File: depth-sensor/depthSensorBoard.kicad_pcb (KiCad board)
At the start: 2 copper layers, 76.2 x 48.3 mm, 28 parts, among them IC1 ATMEGA1284P-M, M1 MountingHole_3.5mm, M2 MountingHole_3.5mm, M3 MountingHole_3.5mm, M4 MountingHole_3.5mm, P1 CONN_02X05, P2 CONN_02X03, P3 CONN_01X04, P4 CONN_01X04, P5 CONN_01X04, P6 CONN_01X04, Q2 Q_NJFET_GSD, U1 AP2112, U2 TCA9545A, Y1 16MHz

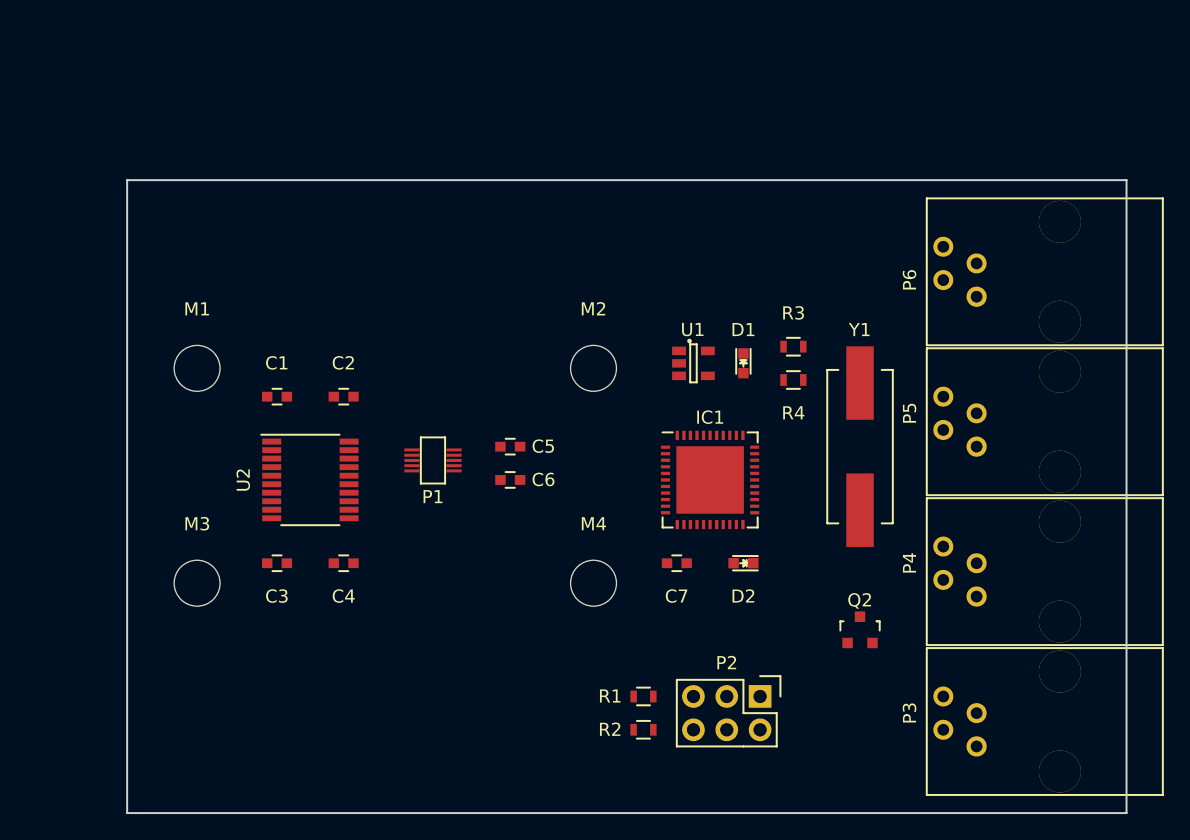
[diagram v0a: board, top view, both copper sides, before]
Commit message: Made PCB smaller
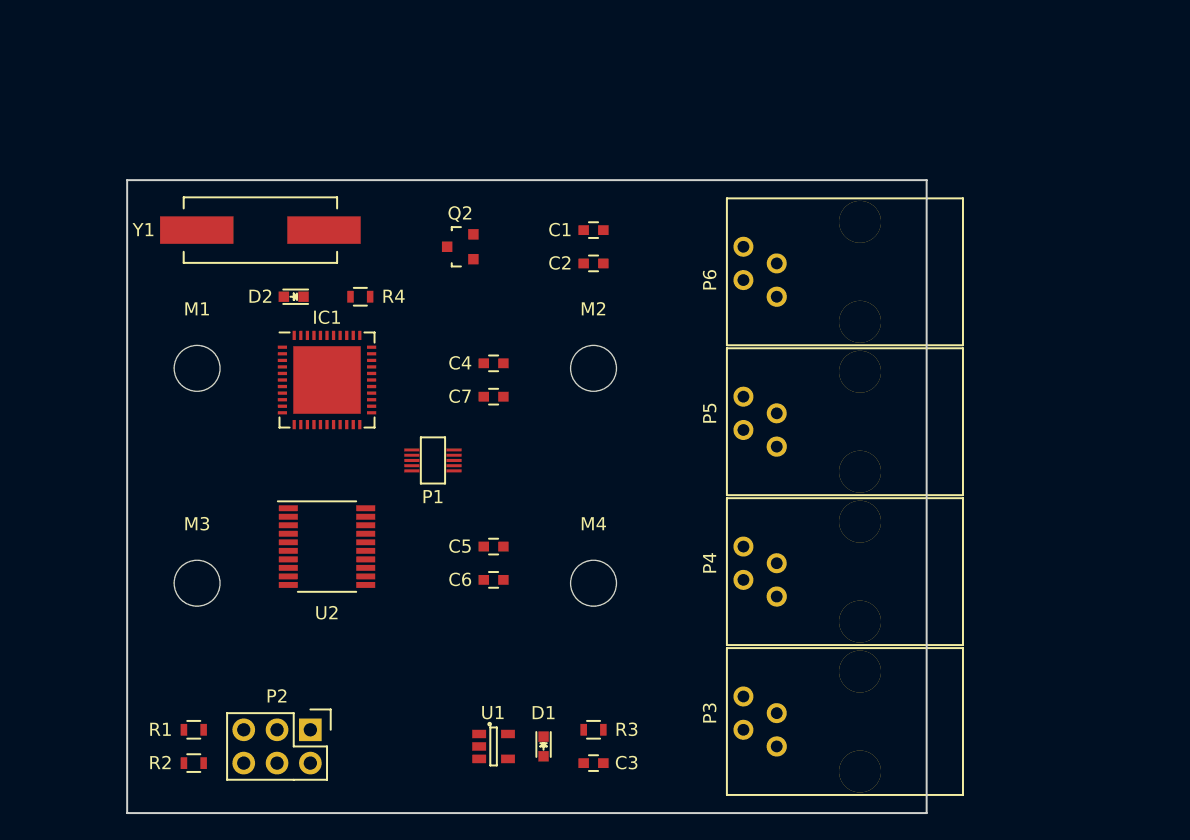
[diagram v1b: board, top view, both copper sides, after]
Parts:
- moved Y1 48.6 mm to (118.1, 110.5), turned to 180 degrees
- moved Q2 42.2 mm to (133.3, 111.8), turned to 90 degrees
- moved D2 39.9 mm to (120.7, 115.6)
- moved P2 34.4 mm to (121.9, 148.6)
- moved R1 34.4 mm to (113.0, 148.6)
- moved R2 34.4 mm to (113.0, 151.1)
- moved R4 33.6 mm to (125.7, 115.6)
- moved D1 32.9 mm to (139.7, 149.9)
- moved R3 32.9 mm to (143.5, 148.6)
- moved U1 32.9 mm to (135.9, 149.9)
- moved IC1 30.2 mm to (123.2, 121.9)
- moved C3 28.5 mm to (143.5, 151.1)
- moved C1 27.3 mm to (143.5, 110.5), turned to 180 degrees
- moved C2 21.6 mm to (143.5, 113.0), turned to 180 degrees
- moved C4 19.0 mm to (135.9, 120.7), turned to 180 degrees
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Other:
- board size 76.2 x 48.3 mm -> 61 x 48.3 mm

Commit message: Rearranged PCB, removed LEDs from depth sensor schematic
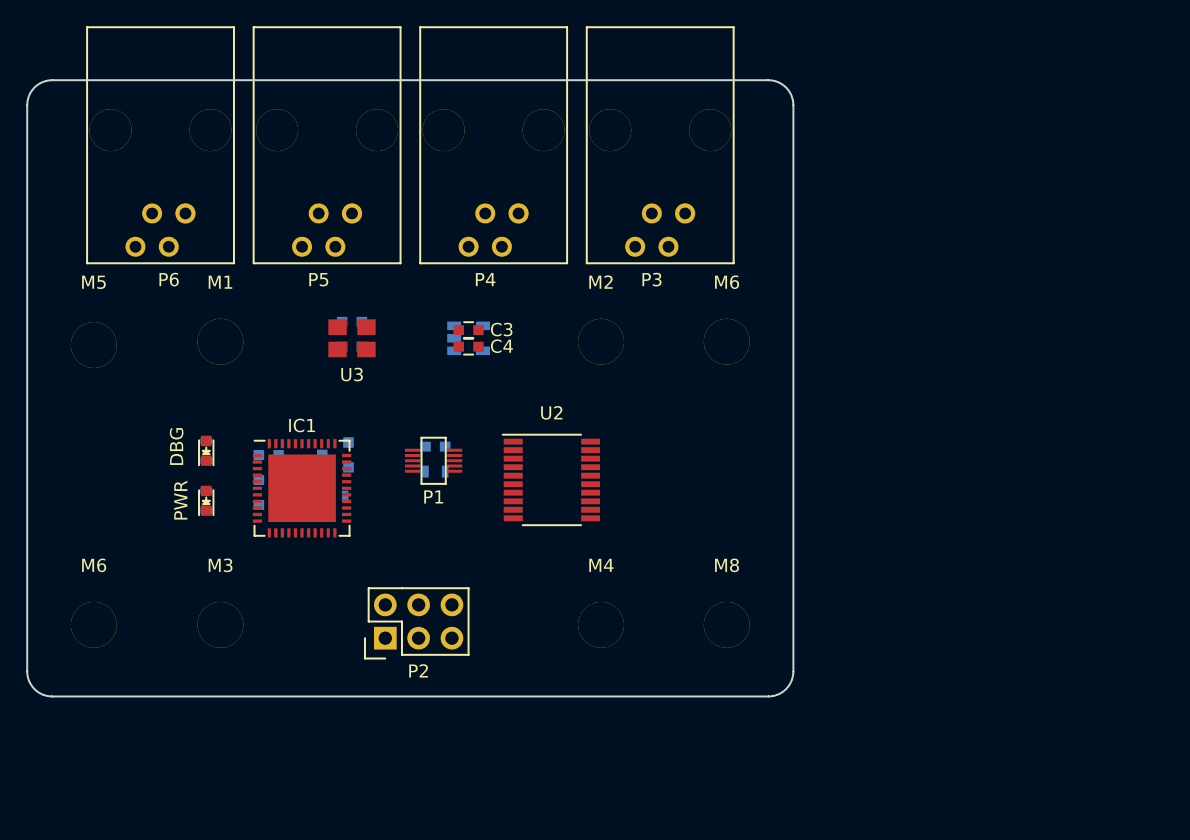
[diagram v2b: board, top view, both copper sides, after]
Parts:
- removed D1, D2: LED, LEDs:LED_0603
- removed R3, R4: 66.5, Resistors_SMD:R_0603
- removed Y1: 16MHz, Crystals:Crystal_HC49-SD_SMD
- added C8: 4.7u, Capacitors_SMD:C_0603, B.Cu at (118.7, 131.4)
- added DBG: LED, LEDs:LED_0603, F.Cu at (114.0, 127.3)
- added M5: MountingHole_3.5mm, Mounting_Holes:MountingHole_3.5mm, F.Cu at (105.4, 119.0)
- added M6: MountingHole_3.5mm, Mounting_Holes:MountingHole_3.5mm, F.Cu at (153.7, 119.0)
- added M6: MountingHole_3.5mm, Mounting_Holes:MountingHole_3.5mm, F.Cu at (105.4, 140.6)
- added M8: MountingHole_3.5mm, Mounting_Holes:MountingHole_3.5mm, F.Cu at (153.7, 140.6)
- added PWR: LED, LEDs:LED_0603, F.Cu at (114.0, 131.1)
- added R5: 65, Resistors_SMD:R_0603, B.Cu at (114.0, 131.1)
- added R6: 65, Resistors_SMD:R_0603, B.Cu at (114.0, 127.3)
- added U3: TSX-3225, robosub_footprints:DFN-4, F.Cu at (125.1, 118.7)
- C1: value 0.1μF -> 100nF; moved to B.Cu
- C2: value 0.1μF -> 18p; moved to B.Cu
- C5: value 100nF -> 18p; moved to B.Cu
- C6, C7: value 30pF -> 100n; moved to B.Cu
- P1: value CONN_02X05 -> Mezzanine-Header
- Q2, R1, R2, U1: moved to B.Cu
- moved P6 45.5 mm to (112.4, 109.2), turned to 180 degrees
- moved P3 41.2 mm to (150.5, 109.2), turned to 180 degrees
- moved P5 36.9 mm to (125.1, 109.2), turned to 180 degrees
- moved P4 35.2 mm to (137.8, 109.2), turned to 180 degrees
- moved C3 34.4 mm to (134.0, 118.1)
- moved U1 31.2 mm to (134.0, 118.7)
- moved R1 27.0 mm to (131.4, 128.9)
- moved R2 23.0 mm to (123.8, 130.8)
- moved C1 20.4 mm to (131.4, 127.0)
- moved C6 19.6 mm to (118.7, 127.6)
- moved C2 18.9 mm to (125.1, 117.5)
- moved C5 18.7 mm to (125.1, 119.4)
- moved Q2 18.5 mm to (123.8, 127.6), turned to 270 degrees
- moved C7 18.3 mm to (118.7, 129.5)
- moved U2 17.9 mm to (140.3, 129.5)
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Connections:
- C1 pad 1: +5V -> Net-(C1-Pad1)
- C1 pad 2: GND -> /DTR
- C2 pad 1: +5V -> Net-(C2-Pad1)
- C5 pad 2: /DTR -> GND
- C6 pad 1: GND -> +5V
- C6 pad 2: Net-(C6-Pad2) -> GND
- C7 pad 1: Net-(C7-Pad1) -> +5V
- IC1 pad 7: Net-(C6-Pad2) -> Net-(C5-Pad1)
- IC1 pad 8: Net-(C7-Pad1) -> Net-(C2-Pad1)
- P3 pad 2: /SCL2 -> /SCL0
- P3 pad 3: /SDA2 -> /SDA0
- P4 pad 2: /SCL3 -> /SCL1
- P4 pad 3: /SDA3 -> /SDA1
- P5 pad 2: /SCL0 -> /SCL2
- P5 pad 3: /SDA0 -> /SDA2
- P6 pad 2: /SCL1 -> /SCL3
- P6 pad 3: /SDA1 -> /SDA3
- R1 pad 2: Net-(C5-Pad1) -> Net-(C1-Pad1)
- R2 pad 2: Net-(C5-Pad1) -> Net-(C1-Pad1)
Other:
- board size 61 x 48.3 mm -> 58.4 x 47 mm

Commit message: Routing completed
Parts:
- moved DBG 0.45 mm to (113.7, 127.0)
- moved PWR 0.45 mm to (113.7, 131.4)
- moved R5 0.45 mm to (113.7, 131.4)
- moved R6 0.45 mm to (113.7, 127.0)
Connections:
- C6 pad 1: +5V -> +3V3
- C7 pad 1: +5V -> +3V3
- C8 pad 1: +5V -> +3V3
- DBG pad 2: /ATMega1284p/DBG_LED -> /DBG_LED
- IC1 pad 17: +5V -> +3V3
- IC1 pad 27: +5V -> +3V3
- IC1 pad 33: /D_LED -> /DBG_LED
- IC1 pad 38: +5V -> +3V3
- IC1 pad 5: +5V -> +3V3
- P2 pad 2: +5V -> +3V3
- PWR pad 2: +5V -> +3V3
- R1 pad 1: +5V -> +3V3
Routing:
- net +3V3: track 0.00 -> 158.3 mm, vias 0 -> 12
- net GND: track 0.00 -> 88.3 mm, vias 0 -> 8
- net /drn: track 0.00 -> 63.8 mm, vias 0 -> 5
- net /SDA3: track 0.00 -> 59.7 mm
- net /SCL3: track 0.00 -> 53.9 mm
- net /SDA2: track 0.00 -> 50.3 mm
- net /SCL2: track 0.00 -> 49.0 mm, vias 0 -> 4
- net /ATMega1284p/SCK: track 0.00 -> 46.3 mm, vias 0 -> 2
- net /ATMega1284p/MISO: track 0.00 -> 46.2 mm
- net /ATMega1284p/~RST: track 0.00 -> 38.9 mm, vias 0 -> 2
- net /~INT: track 0.00 -> 36.7 mm
- net /SCL: track 0.00 -> 35.2 mm, vias 0 -> 2
- net /SDA: track 0.00 -> 32.5 mm, vias 0 -> 2
- net /ATMega1284p/MOSI: track 0.00 -> 29.6 mm, vias 0 -> 4
- net /SCL1: track 0.00 -> 29.6 mm, vias 0 -> 2
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- added copper zone on F.Cu, net +3V3
- added copper zone on B.Cu, net GND
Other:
- net class Default: clearance 0.2 -> 0.1524; trace_width 0.25 -> 0.1524; via_dia 0.6 -> 0.508; via_drill 0.4 -> 0.3302
- rule trace_clearance: 0.2 -> 0.1524
- rule trace_min: 0.2 -> 0.1524
- rule via_min_size: 0.4 -> 0.508

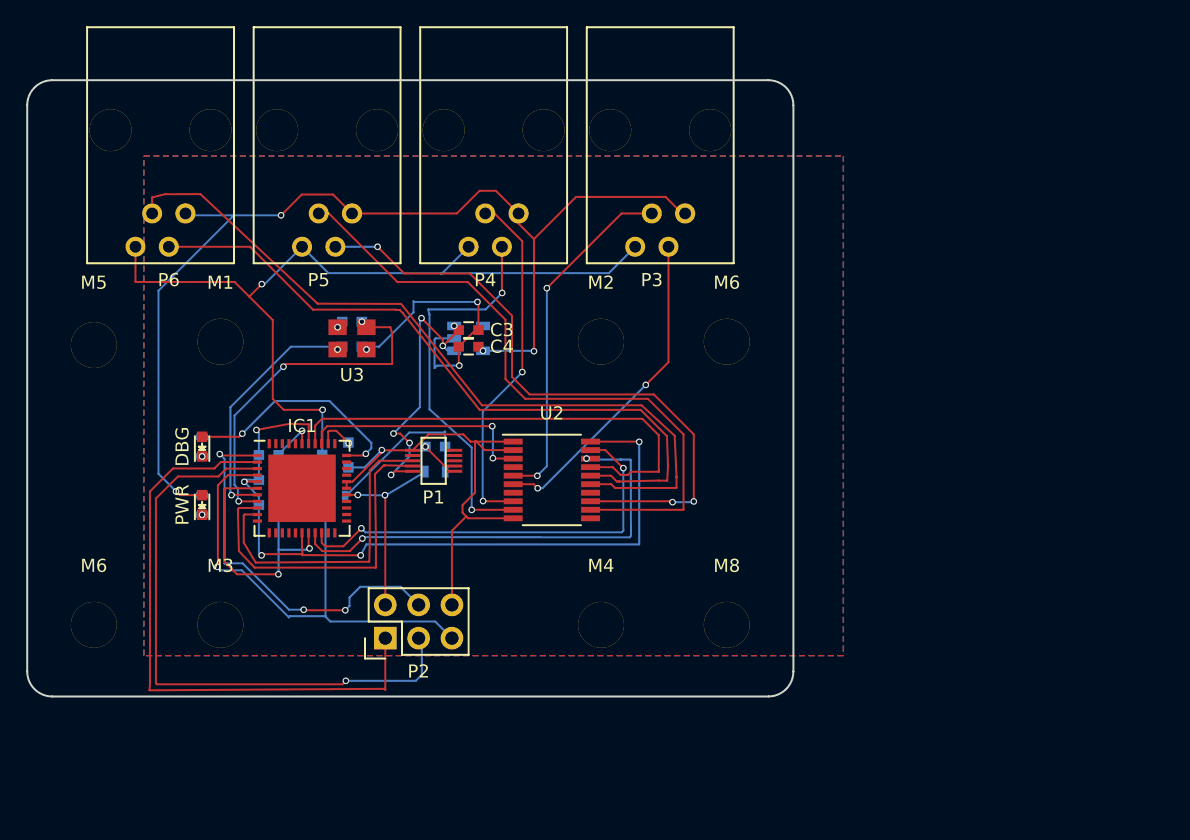
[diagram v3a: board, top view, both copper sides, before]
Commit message: Changed to just GND fill
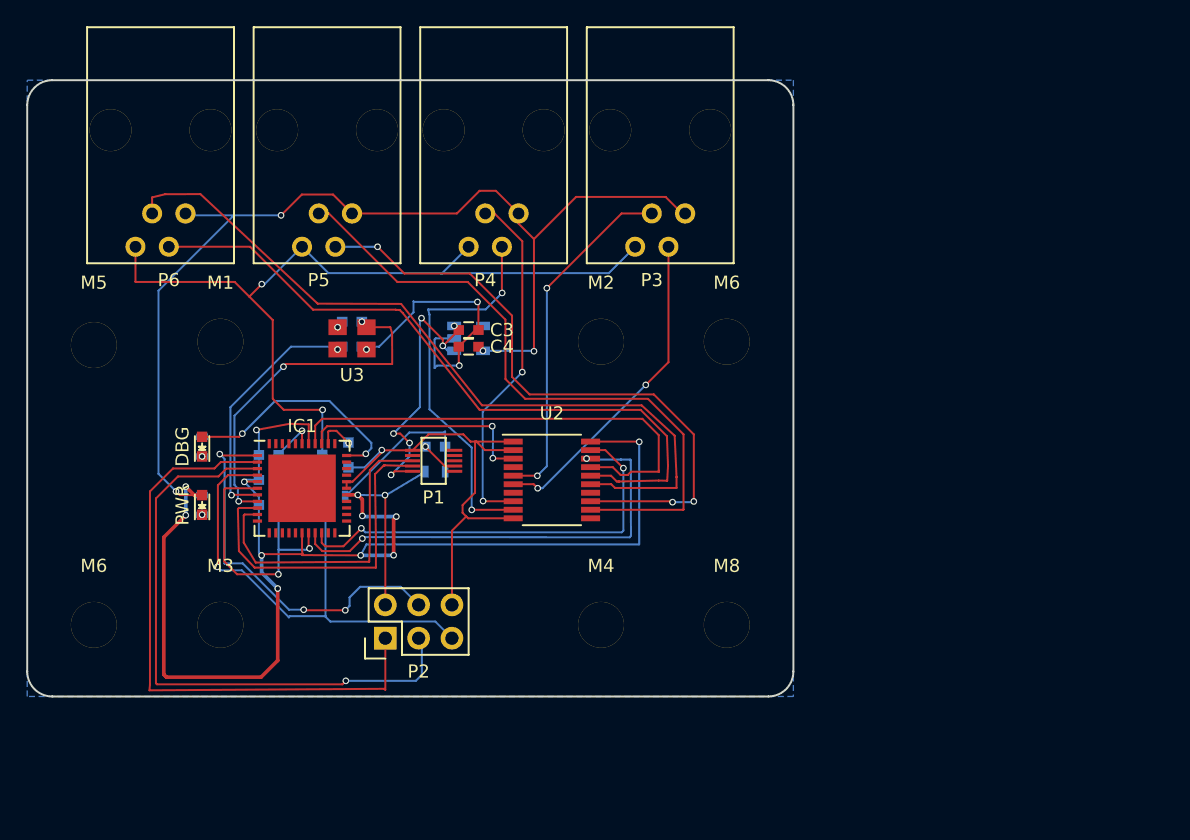
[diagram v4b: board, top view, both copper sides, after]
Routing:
- net +3V3: track 158.3 -> 202.6 mm, vias 12 -> 18
- removed copper zone on F.Cu, net +3V3
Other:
- net class PWR added: clearance 0.1524, trace_width 0.2788, via_dia 0.508, via_drill 0.3302
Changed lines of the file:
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@@
     (thickness 1.6)
     (drawings 10)
-    (tracks 478)
+    (tracks 503)
     (zones 0)
     (modules 33)
@@
     (uvia_dia 0.3)
     (uvia_drill 0.1)
-    (add_net +3V3)
-    (add_net +5V)
     (add_net /ATMega1284p/MISO)
     (add_net /ATMega1284p/MOSI)
@@
     (add_net /~INT)
     (add_net /~RST)
-    (add_net GND)
     (add_net "Net-(C1-Pad1)")
     (add_net "Net-(C2-Pad1)")
@@
     (add_net "Net-(U2-Pad4)")
     (add_net "Net-(U2-Pad7)")
+  )
+  (net_class PWR ""
+    (clearance 0.1524)
+    (trace_width 0.2788)
+    (via_dia 0.508)
+    (via_drill 0.3302)
+    (uvia_dia 0.3)
+    (uvia_drill 0.1)
+    (add_net +3V3)
+    (add_net +5V)
+    (add_net GND)
   )
   (module Resistors_SMD:R_0603 (layer B.Cu)
@@
   (via (at 121.285 125.7935) (size 0.508) (drill 0.3302) (layers F.Cu B.Cu) (net 2))
   (segment (start 119.495 127.5835) (end 119.495 127.635) (width 0.1524) (layer B.Cu) (net 2))
+  (segment (start 124.685 130.675) (end 125.5315 130.675) (width 0.2788) (layer F.Cu) (net 3))
+  (segment (start 125.5315 130.675) (end 125.8824 131.0259) (width 0.2788) (layer F.Cu) (net 3))
+  (segment (start 128.25984 135.29056) (end 125.76048 135.29056) (width 0.2788) (layer B.Cu) (net 3))
+  (segment (start 128.27 135.2804) (end 128.25984 135.29056) (width 0.2788) (layer B.Cu) (net 3))
+  (via (at 128.27 135.2804) (size 0.508) (drill 0.3302) (layers F.Cu B.Cu) (net 3))
+  (segment (start 128.27 132.5372) (end 128.27 135.2804) (width 0.2788) (layer F.Cu) (net 3))
+  (segment (start 128.4732 132.334) (end 128.27 132.5372) (width 0.2788) (layer F.Cu) (net 3))
+  (via (at 128.4732 132.334) (size 0.508) (drill 0.3302) (layers F.Cu B.Cu) (net 3))
+  (segment (start 125.9332 132.334) (end 128.4732 132.334) (width 0.2788) (layer B.Cu) (net 3))
+  (segment (start 125.8824 132.2832) (end 125.9332 132.334) (width 0.2788) (layer B.Cu) (net 3))
+  (via (at 125.8824 132.2832) (size 0.508) (drill 0.3302) (layers F.Cu B.Cu) (net 3))
+  (segment (start 125.8824 131.0259) (end 125.8824 132.2832) (width 0.2788) (layer F.Cu) (net 3))
+  (segment (start 113.665 130.6957) (end 113.0681 130.6957) (width 0.2788) (layer F.Cu) (net 3))
+  (segment (start 118.20144 136.59104) (end 118.20144 135.29056) (width 0.2788) (layer B.Cu) (net 3))
+  (segment (start 119.4308 137.8204) (end 118.20144 136.59104) (width 0.2788) (layer B.Cu) (net 3))
+  (via (at 119.4308 137.8204) (size 0.508) (drill 0.3302) (layers F.Cu B.Cu) (net 3))
+  (segment (start 119.4308 143.3068) (end 119.4308 137.8204) (width 0.2788) (layer F.Cu) (net 3))
+  (segment (start 118.1608 144.5768) (end 119.4308 143.3068) (width 0.2788) (layer F.Cu) (net 3))
+  (segment (start 110.9472 144.5768) (end 118.1608 144.5768) (width 0.2788) (layer F.Cu) (net 3))
+  (segment (start 110.744 144.3736) (end 110.9472 144.5768) (width 0.2788) (layer F.Cu) (net 3))
+  (segment (start 110.744 133.9088) (end 110.744 144.3736) (width 0.2788) (layer F.Cu) (net 3))
+  (segment (start 112.4204 132.2324) (end 110.744 133.9088) (width 0.2788) (layer F.Cu) (net 3))
+  (via (at 112.4204 132.2324) (size 0.508) (drill 0.3302) (layers F.Cu B.Cu) (net 3))
+  (segment (start 112.4204 130.048) (end 112.4204 132.2324) (width 0.2788) (layer B.Cu) (net 3))
+  (via (at 112.4204 130.048) (size 0.508) (drill 0.3302) (layers F.Cu B.Cu) (net 3))
+  (segment (start 113.0681 130.6957) (end 112.4204 130.048) (width 0.2788) (layer F.Cu) (net 3))
   (segment (start 113.665 130.6957) (end 111.96066 130.6957) (width 0.1524) (layer F.Cu) (net 3))
   (segment (start 110.3376 115.1128) (end 116.08816 109.36224) (width 0.1524) (layer B.Cu) (net 3))
@@
   (segment (start 111.96066 130.6957) (end 111.67872 130.41376) (width 0.1524) (layer F.Cu) (net 3))
   (segment (start 117.995 131.445) (end 117.995 135.08412) (width 0.1524) (layer B.Cu) (net 3))
+  (segment (start 117.995 135.08412) (end 118.20144 135.29056) (width 0.1524) (layer B.Cu) (net 3))
   (segment (start 121.321762 135.19758) (end 121.321762 135.270199) (width 0.1524) (layer F.Cu) (net 3))
+  (via (at 118.20144 135.29056) (size 0.508) (drill 0.3302) (layers F.Cu B.Cu) (net 3))
+  (segment (start 118.20144 135.29056) (end 118.29442 135.19758) (width 0.1524) (layer F.Cu) (net 3))
   (segment (start 118.29442 135.19758) (end 121.321762 135.19758) (width 0.1524) (layer F.Cu) (net 3))
-  (segment (start 118.20144 135.29056) (end 118.29442 135.19758) (width 0.1524) (layer F.Cu) (net 3))
-  (via (at 118.20144 135.29056) (size 0.508) (drill 0.3302) (layers F.Cu B.Cu) (net 3))
-  (segment (start 117.995 135.08412) (end 118.20144 135.29056) (width 0.1524) (layer B.Cu) (net 3))
   (segment (start 125.095 109.22) (end 133.096 109.22) (width 0.1524) (layer F.Cu) (net 3))
   (segment (start 136.0678 107.4928) (end 137.795 109.22) (width 0.1524) (layer F.Cu) (net 3))
@@
   (segment (start 117.995 127.635) (end 117.995 129.54) (width 0.1524) (layer B.Cu) (net 3))
   (segment (start 130.695 128.905) (end 127.67056 130.71856) (width 0.1524) (layer B.Cu) (net 3))
-  (segment (start 125.5315 130.675) (end 124.685 130.675) (width 0.1524) (layer F.Cu) (net 3))
   (segment (start 125.5395 130.683) (end 125.5315 130.675) (width 0.1524) (layer F.Cu) (net 3))
   (via (at 125.5395 130.683) (size 0.508) (drill 0.3302) (layers F.Cu B.Cu) (net 3))
@@
   (via (at 126.1491 127.5461) (size 0.508) (drill 0.3302) (layers F.Cu B.Cu) (net 61))
   (segment (start 126.0202 127.675) (end 126.1491 127.5461) (width 0.1524) (layer F.Cu) (net 61))
-  (zone (net 3) (net_name +3V3) (layer F.Cu) (hatch edge 0.508)
-    (connect_pads (clearance 0.508))
-    (min_thickness 0.254)
-    (fill yes (arc_segments 16) (thermal_gap 0.508) (thermal_bridge_width 0.508))
-    (polygon
-      (pts
-        (xy 162.56 142.9385) (xy 109.22 142.9385) (xy 109.22 104.8385) (xy 162.56 104.8385)
-      )
-    )
-  )
   (zone (net 2) (net_name GND) (layer B.Cu) (hatch edge 0.508)
     (connect_pads (clearance 0.508))
@@
     (polygon
       (pts
-        (xy 162.56 142.9385) (xy 109.22 142.9385) (xy 109.22 104.8385) (xy 162.56 104.8385)
+        (xy 158.75 146.05) (xy 100.33 146.05) (xy 100.33 99.06) (xy 158.75 99.06)
       )
     )
